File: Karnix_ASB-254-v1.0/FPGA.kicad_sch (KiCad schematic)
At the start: 48 parts, among them U5 LFE5U-25F-BG256C, U7 W25Q128JVPIQ, Y2 25 MHz

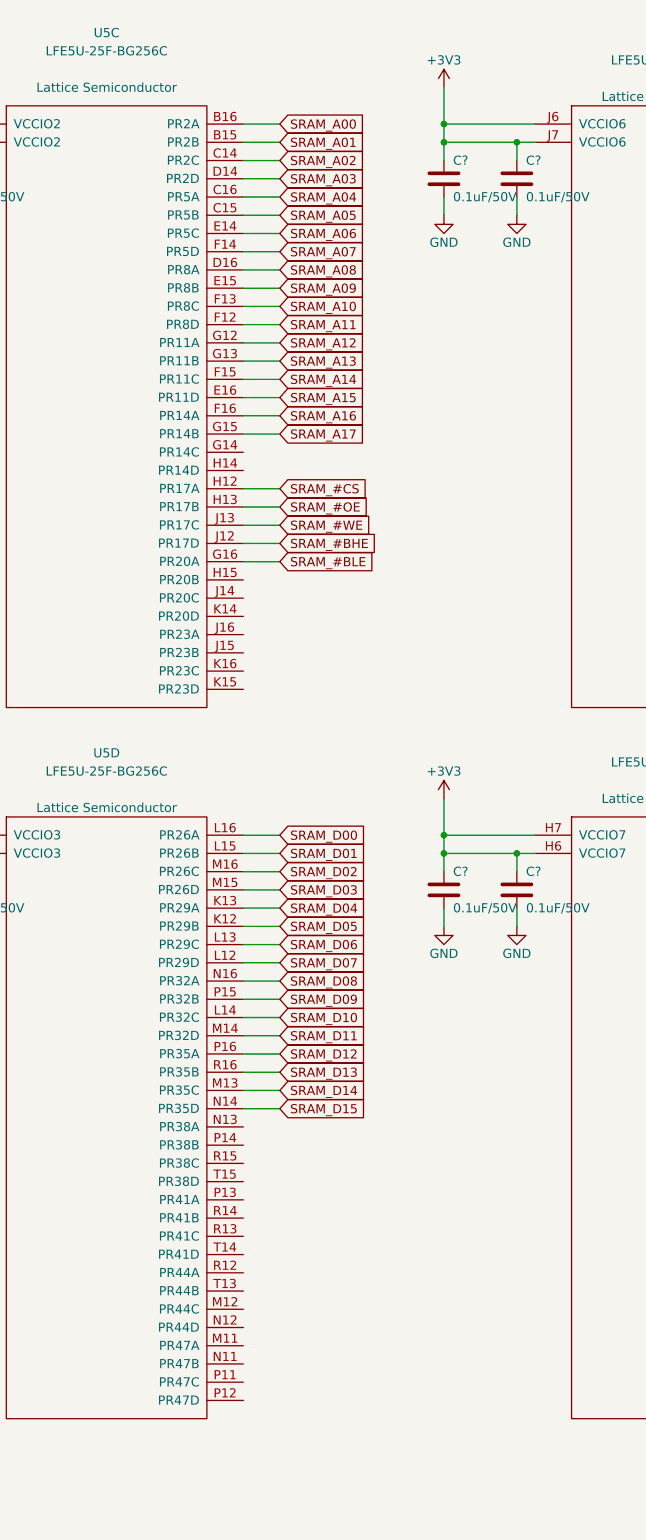
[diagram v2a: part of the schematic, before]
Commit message: Move SRAM signals to some other pins on FPGA to ease routing
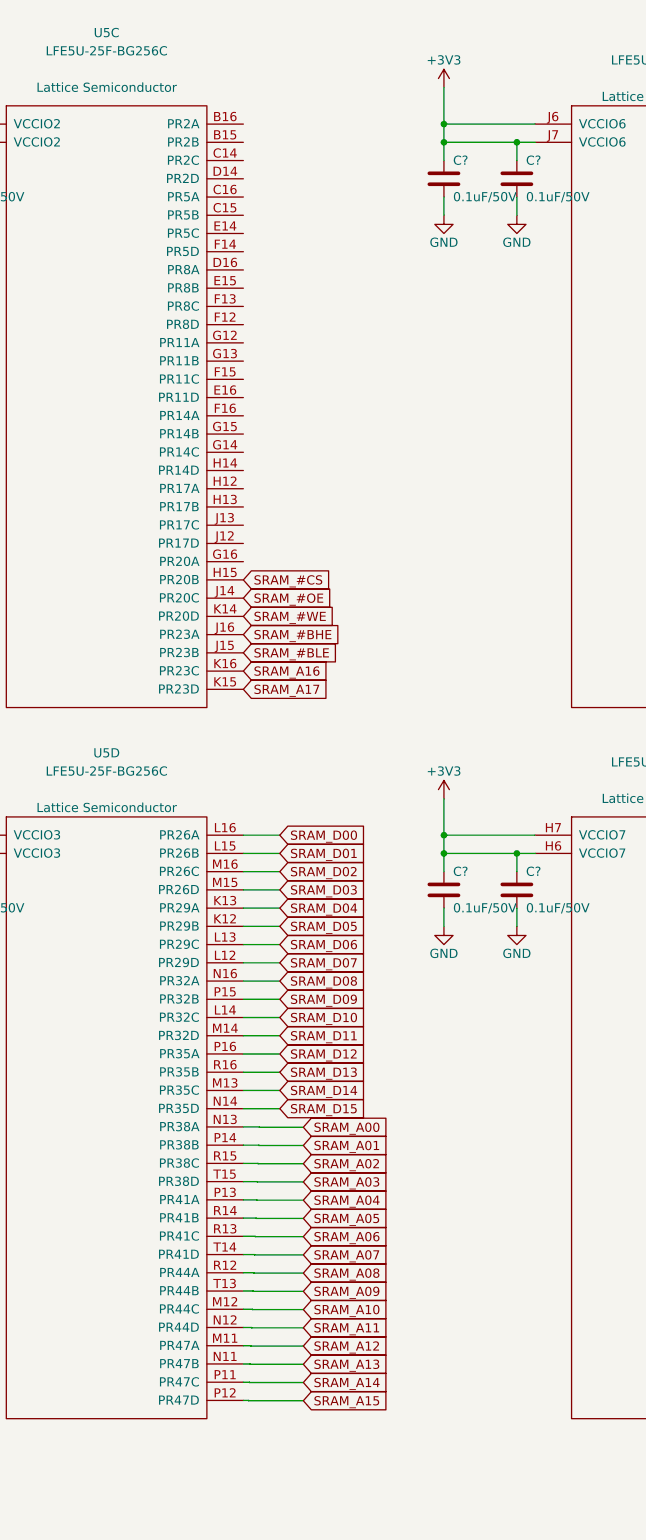
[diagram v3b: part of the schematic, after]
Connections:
- net SRAM_#BHE: now also U5.J16 (PR23A); no longer U5.J12 (PR17D)
- net SRAM_#BLE: now also U5.J15 (PR23B); no longer U5.G16 (PR20A)
- net SRAM_#CS: now also U5.H15 (PR20B); no longer U5.H12 (PR17A)
- net SRAM_#OE: now also U5.J14 (PR20C); no longer U5.H13 (PR17B)
- net SRAM_#WE: now also U5.K14 (PR20D); no longer U5.J13 (PR17C)
- net SRAM_A00: now also U5.N13 (PR38A); no longer U5.B16 (PR2A)
- net SRAM_A01: now also U5.P14 (PR38B); no longer U5.B15 (PR2B)
- net SRAM_A02: now also U5.R15 (PR38C); no longer U5.C14 (PR2C)
- net SRAM_A03: now also U5.T15 (PR38D); no longer U5.D14 (PR2D)
- net SRAM_A04: now also U5.P13 (PR41A); no longer U5.C16 (PR5A)
- net SRAM_A05: now also U5.R14 (PR41B); no longer U5.C15 (PR5B)
- net SRAM_A06: now also U5.R13 (PR41C); no longer U5.E14 (PR5C)
- net SRAM_A07: now also U5.T14 (PR41D); no longer U5.F14 (PR5D)
- net SRAM_A08: now also U5.R12 (PR44A); no longer U5.D16 (PR8A)
- net SRAM_A09: now also U5.T13 (PR44B); no longer U5.E15 (PR8B)
- net SRAM_A10: now also U5.M12 (PR44C); no longer U5.F13 (PR8C)
- net SRAM_A11: now also U5.N12 (PR44D); no longer U5.F12 (PR8D)
- net SRAM_A12: now also U5.M11 (PR47A); no longer U5.G12 (PR11A)
- net SRAM_A13: now also U5.N11 (PR47B); no longer U5.G13 (PR11B)
- net SRAM_A14: now also U5.P11 (PR47C); no longer U5.F15 (PR11C)
- net SRAM_A15: now also U5.P12 (PR47D); no longer U5.E16 (PR11D)
- net SRAM_A16: now also U5.K16 (PR23C); no longer U5.F16 (PR14A)
- net SRAM_A17: now also U5.K15 (PR23D); no longer U5.G15 (PR14B)
